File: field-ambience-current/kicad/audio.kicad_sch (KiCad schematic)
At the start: 24 parts, among them J6 Speaker L (PUI AS04008PS, 4R 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, J7 Speaker R (PUI AS04008PS, 4R 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, U3 PCM5102A I²S DAC (TSSOP-20), U4 PAM8403H Class-D Stereo Amp (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

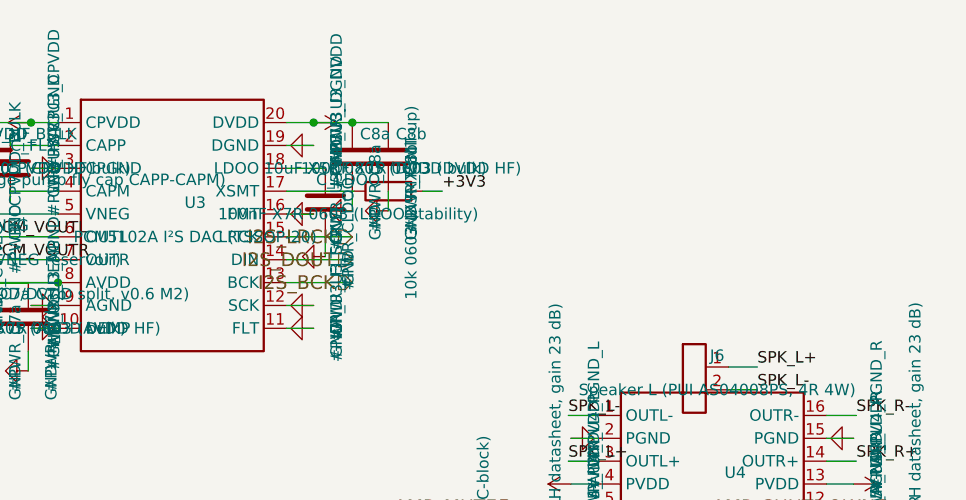
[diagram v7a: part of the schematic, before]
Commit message: v0.6.3-r5 N1-Fix: PCM5102A XSMT via MCP23017 GPA5 GPIO control
User-Wunsch: "lieber direkt haben als nicht haben" — explizite GPIO-
gesteuerte Pop-Suppression für PCM5102A statt nur statischem Pull-Up.

Hardware-Änderungen:

audio.kicad_sch (PCM5102A Pin 17 XSMT):
- BEFORE: R_XSMT 10k pull-up zu DVDD (chip statisch un-muted)
- AFTER:
  - R_XSMT_PD 10k pull-down zu GND (boot-safe default LOW = muted)
  - hier-input PCM_XSMT (vom MCP23017 via I²C-Steuerung)
  → Während Pico-Reset/Boot: XSMT bleibt LOW (DAC stumm), egal was
     der PCM5102A intern macht.

mcp.kicad_sch (MCP23017 GPA5 = Pin 26):
- BEFORE: NC_GPA5 reserve label (Pin ungenutzt)
- AFTER: hier-output PCM_XSMT (drives PCM5102A XSMT via PCM_XSMT net)

root.kicad_sch:
- MCP-Sheet-Box bekommt PCM_XSMT output pin (right side y=215)
- Audio-Sheet-Box bekommt PCM_XSMT input pin (left side y=240)
- Audio-Sheet-Box-Höhe von 50 → 55 erweitert (für zusätzlichen Pin)
- Cross-Sheet Label-Bridge PCM_XSMT zwischen MCP und Audio

Firmware-Sequenz (dokumentiert in SPEC v0.6.3-r5):
1. Boot: MCP23017-Pins default Input → R_XSMT_PD zieht XSMT LOW → PCM stumm
2. I²C-Init: MCP23017 GPA5 als Output, default 0 (XSMT bleibt LOW)
3. Power-Rails stabilisieren (~50 ms)
4. PAM8403 enable: GP28 (MUTE) HIGH, 100 ms später GP27 (SHDN) HIGH
5. PCM un-mute: MCP GPA5 HIGH → PCM_XSMT = +3V3 → DAC un-muted
6. → kein Pop am Speaker, kein DAC-Hochfahr-Knack

SPEC §7 MCP23017 Pin-Tabelle aktualisiert: GPA5 dokumentiert als
PCM_XSMT-Control, nicht mehr als reserve.

Analyzer-Status: 0 functional errors, 18 warnings (one less than r4 weil
NC_GPA5 label weg ist), 90 components (R_XSMT durch R_XSMT_PD ersetzt,
keine net-Change), 119 nets.

Verified via analyzer pin_nets:
- U3 Pin 17 (XSMT) → PCM_XSMT ✓
- U2 Pin 26 (GPA5) → PCM_XSMT ✓
- R_XSMT_PD pin1 = PCM_XSMT, pin2 = GND ✓

Damit ist Pop-Suppression jetzt belt-and-suspenders:
- Boot: PAM /MUTE LOW (R_MUTE_PD) + /SHDN LOW (R_SHDN_PD) + PCM XSMT LOW
- Operation: alle drei HIGH durch Firmware
- Shutd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
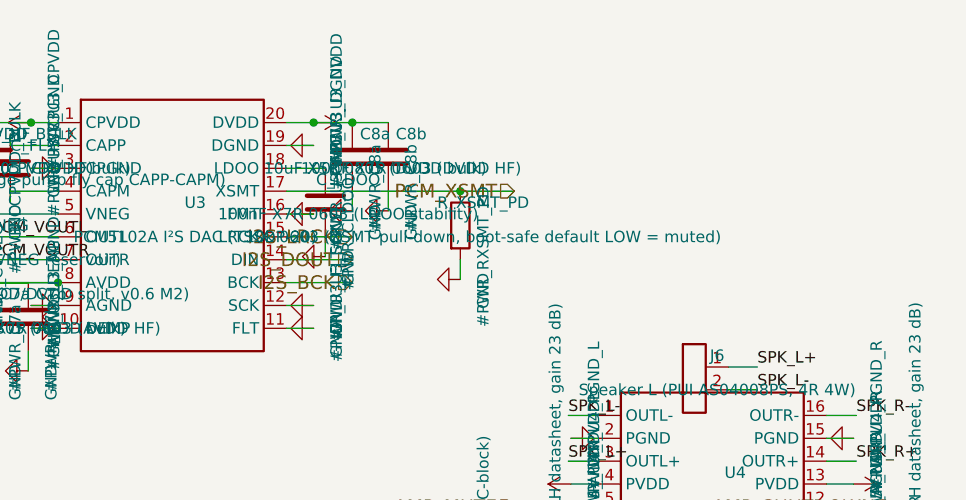
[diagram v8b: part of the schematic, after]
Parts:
- removed R_XSMT: 10k 0603 (XSMT pull-up), Resistor_SMD:R_0603_1608Metric, symbol Device:R
- added R_XSMT_PD: 10k 0603 (XSMT pull-down, boot-safe default LOW =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, Resistor_SMD:R_0603_1608Metric, symbol Device:R
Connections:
- net GND: now also R_XSMT_PD.2
- net PCM_XSMT: now reaches U3.17 (XSMT)
- net PCM_XSMT: now also R_XSMT_PD.1
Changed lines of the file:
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@@
       (project "field_ambience"
         (path "/66fcdc89-be06-4d61-a855-abf9641d963c" (reference "#PWR_U3_FMT") (unit 1)))))
-  (symbol (lib_id "Device:R") (at 124 96.19 90) (unit 1)
-    (in_bom yes) (on_board yes) (dnp no)
-      (property "Reference" "R_XSMT" (at 126.54 93.64999999999999 0)
-        (effects (font (size 1.27 1.27))))
-      (property "Value" "10k 0603 (XSMT pull-up)" (at 126.54 97.46 0)
-        (effects (font (size 1.27 1.27))))
-      (property "Footprint" "Resistor_SMD:R_0603_1608Metric" (at 124 96.19 0)
-        (effects (font (size 1.27 1.27)) hide))
-      (property "Datasheet" "~" (at 124 96.19 0)
-        (effects (font (size 1.27 1.27)) hide))
-      (property "MPN" "RC0603FR-0710KL" (at 126.54 100.0 0)
-        (effects (font (size 1.27 1.27)) hide))
-      (property "LCSC" "C25804" (at 126.54 101.27 0)
-        (effects (font (size 1.27 1.27)) hide))
-    (instances
-      (project "field_ambience"
-        (path "/66fcdc89-be06-4d61-a855-abf9641d963c" (reference "R_XSMT") (unit 1)))))
+  (symbol (lib_id "Device:R") (at 132 100.0 0) (unit 1)
+    (in_bom yes) (on_board yes) (dnp no)
+      (property "Reference" "R_XSMT_PD" (at 134.54 97.46 0)
+        (effects (font (size 1.27 1.27))))
+      (property "Value" "10k 0603 (XSMT pull-down, boot-safe default LOW = muted)" (at 134.54 101.27 0)
+        (effects (font (size 1.27 1.27))))
+      (property "Footprint" "Resistor_SMD:R_0603_1608Metric" (at 132 100.0 0)
+        (effects (font (size 1.27 1.27)) hide))
+      (property "Datasheet" "~" (at 132 100.0 0)
+        (effects (font (size 1.27 1.27)) hide))
+      (property "MPN" "RC0603FR-0710KL" (at 134.54 103.81 0)
+        (effects (font (size 1.27 1.27)) hide))
+      (property "LCSC" "C25804" (at 134.54 105.08 0)
+        (effects (font (size 1.27 1.27)) hide))
+    (instances
+      (project "field_ambience"
+        (path "/66fcdc89-be06-4d61-a855-abf9641d963c" (reference "R_XSMT_PD") (unit 1)))))
+  (symbol (lib_id "Power:GND") (at 132 106.0 270) (unit 1)
+    (in_bom yes) (on_board yes) (dnp no)
+      (property "Reference" "#PWR_RXSMT_PD" (at 134.54 103.46 0)
+        (effects (font (size 1.27 1.27))))
+      (property "Value" "GND" (at 134.54 107.27 0)
+        (effects (font (size 1.27 1.27))))
+      (property "Footprint" "" (at 132 106.0 0)
+        (effects (font (size 1.27 1.27)) hide))
+      (property "Datasheet" "~" (at 132 106.0 0)
+        (effects (font (size 1.27 1.27)) hide))
+    (instances
+      (project "field_ambience"
+        (path "/66fcdc89-be06-4d61-a855-abf9641d963c" (reference "#PWR_RXSMT_PD") (unit 1)))))
   (symbol (lib_id "Device:C") (at 117 97.46 0) (unit 1)
     (in_bom yes) (on_board yes) (dnp no)
@@
     (stroke (width 0) (type default))
 )
-  (wire (pts (xy 112.7 96.19) (xy 120.19 96.19))
-    (stroke (width 0) (type default))
-)
-  (wire (pts (xy 127.81 96.19) (xy 130 96.19))
+  (wire (pts (xy 112.7 96.19) (xy 132 96.19))
+    (stroke (width 0) (type default))
+)
+  (wire (pts (xy 132 96.19) (xy 138 96.19))
+    (stroke (width 0) (type default))
+)
+  (wire (pts (xy 132 103.81) (xy 132 106.0))
     (stroke (width 0) (type default))
 )
@@
   (junction (at 80 106.35) (diameter 0) (color 0 0 0 0)
 )
+  (junction (at 132 96.19) (diameter 0) (color 0 0 0 0)
+)
   (junction (at 115.7 88.57) (diameter 0) (color 0 0 0 0)
 )
@@
 )
   (label "PCM_VOUTR" (at 80 103.80999999999999 0) (fields_autoplaced)
-    (effects (font (size 1.27 1.27)) (justify left bottom))
-)
-  (label "+3V3" (at 130 96.19 0) (fields_autoplaced)
     (effects (font (size 1.27 1.27)) (justify left bottom))
 )
@@
     (effects (font (size 1.524 1.524)) (justify right))
 )
+  (hierarchical_label "PCM_XSMT" (shape input) (at 138 96.19 180)
+    (effects (font (size 1.524 1.524)) (justify right))
+)
